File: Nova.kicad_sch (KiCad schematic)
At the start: 35 parts, among them J1 MEM2067-02-180-00-A, J2 Breakout, J3 TC2030-NL, Q1 BC817, Q2 BC817, SW1 PTS636 SK25J, U1 STM32L552RCT6, U2 W25N01GVZEIG, U3 FM24CL16B, Y1 ECS-160-9-33B-CTP-TR, Y2 ECS-.327-9-12R-TR

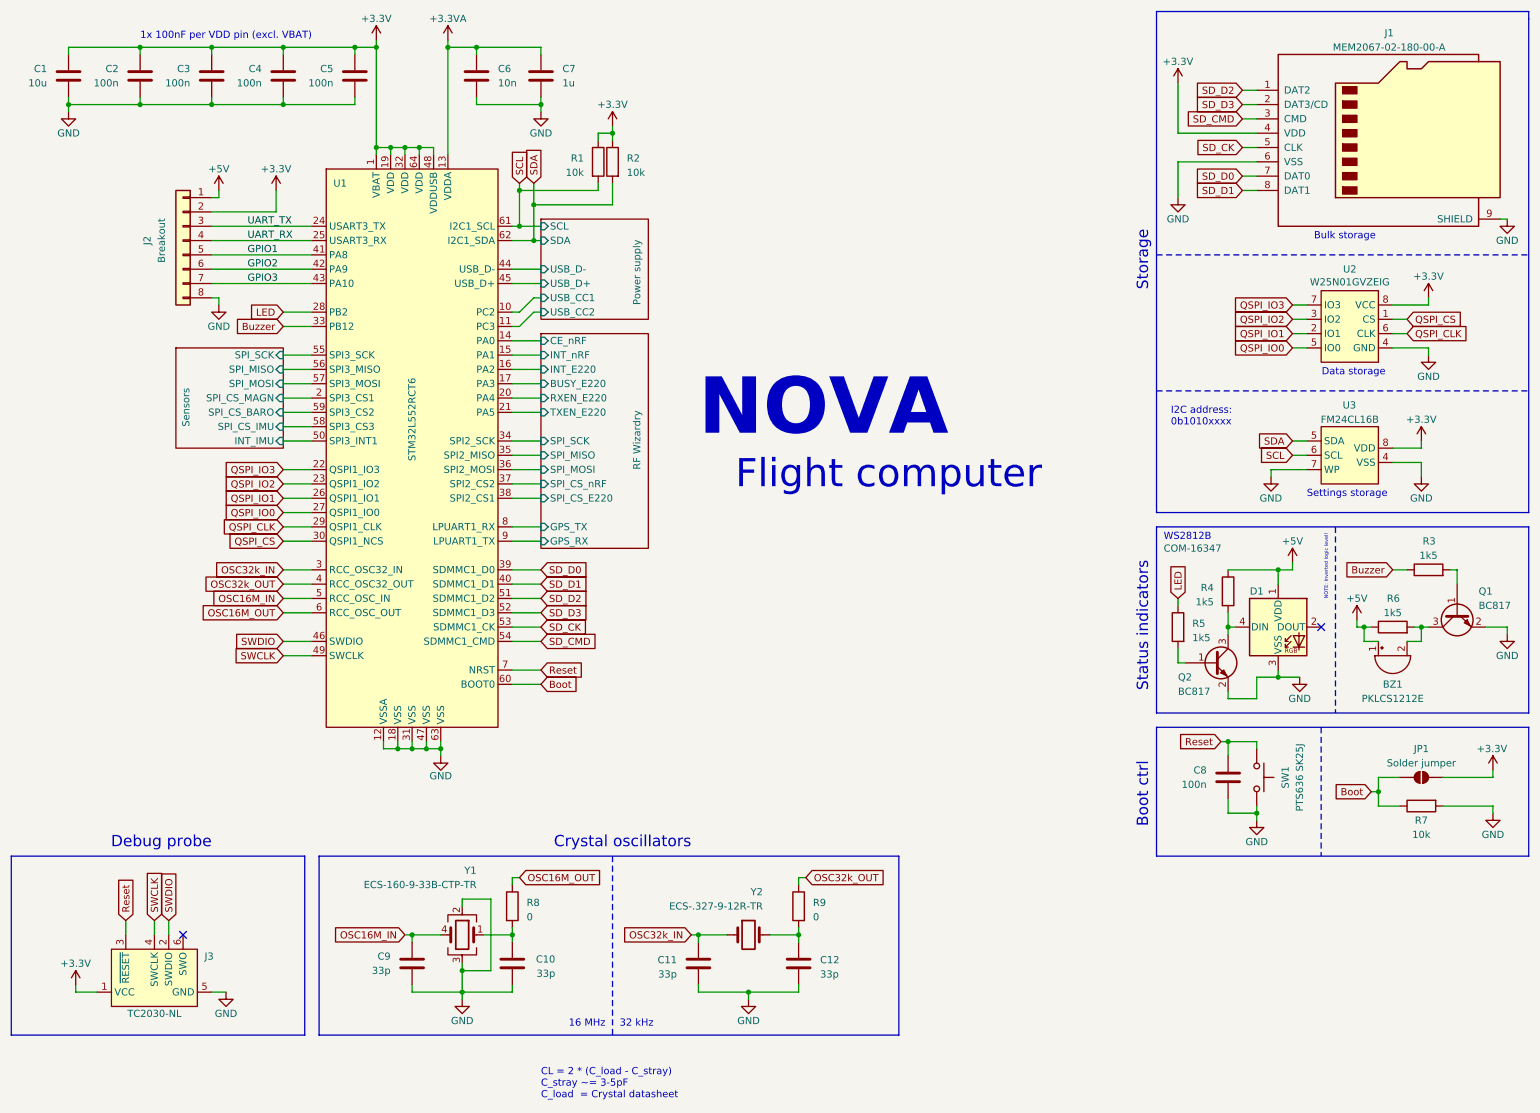
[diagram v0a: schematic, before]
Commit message: :children_crossing: Add test pads and assign footprints
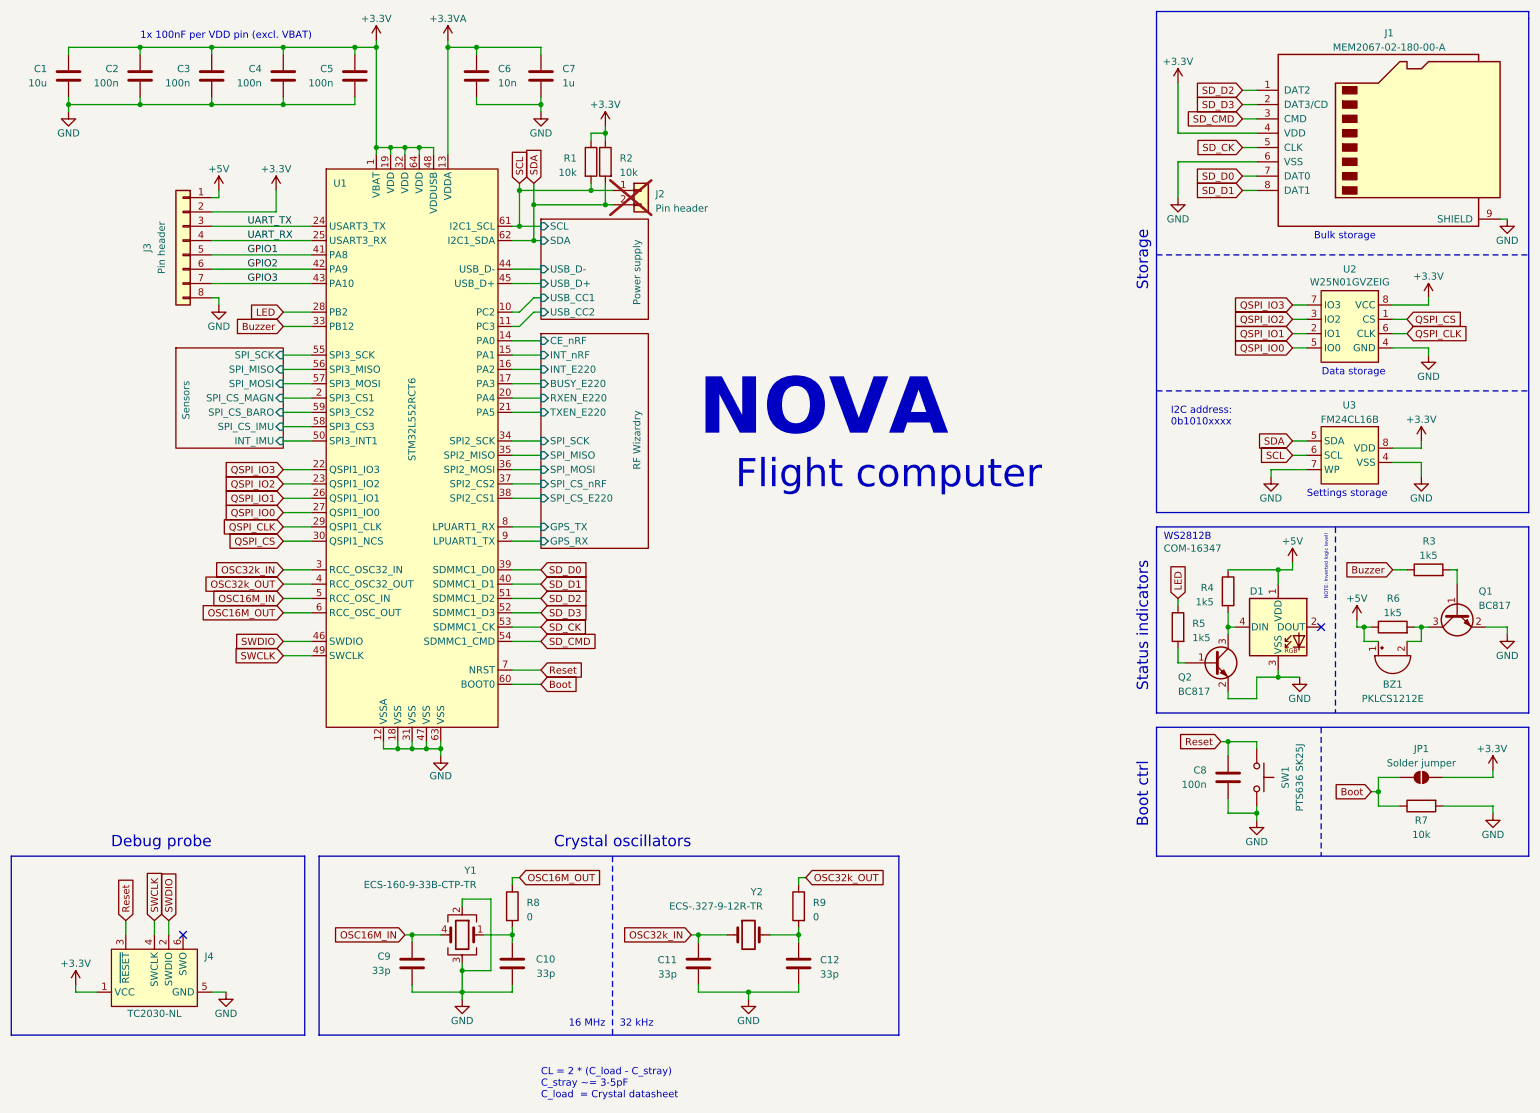
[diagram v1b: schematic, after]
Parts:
- added J2: Pin header, Connector_PinHeader_2.54mm:PinHeader_1x02_P2.54mm_Vertical, symbol Connector_Generic:Conn_01x02
- J3: renamed from J2; value Breakout -> Pin header
- U3: footprint (none) -> Package_SO:SOIC-8_3.9x4.9mm_P1.27mm
- renumbered J3 to J4
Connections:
- net SCL: now also J2.1 (Pin_1)
- net SDA: now also J2.2 (Pin_2)
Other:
- moved on the sheet: R1, R2
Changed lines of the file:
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@@
   (junction (at 93.98 184.15) (diameter 0) (color 0 0 0 0)
   )
+  (junction (at 119.38 48.26) (diameter 0) (color 0 0 0 0)
+  )
   (junction (at 85.09 177.8) (diameter 0) (color 0 0 0 0)
   )
@@
   (junction (at 229.87 123.19) (diameter 0) (color 0 0 0 0)
   )
+  (junction (at 119.38 35.56) (diameter 0) (color 0 0 0 0)
+  )
   (junction (at 229.87 143.51) (diameter 0) (color 0 0 0 0)
   )
@@
   (junction (at 104.14 45.72) (diameter 0) (color 0 0 0 0)
   )
+  (junction (at 116.84 45.72) (diameter 0) (color 0 0 0 0)
+  )
   (junction (at 256.54 152.4) (diameter 0) (color 0 0 0 0)
   )
@@
   )
   (junction (at 36.83 20.32) (diameter 0) (color 0 0 0 0)
-  )
-  (junction (at 120.65 35.56) (diameter 0) (color 0 0 0 0)
   )
   (junction (at 86.36 38.1) (diameter 0) (color 0 0 0 0)
@@
     (stroke (width 0) (type default))
   )
-  (wire (pts (xy 118.11 35.56) (xy 118.11 36.83))
-    (stroke (width 0) (type default))
-  )
   (wire (pts (xy 102.87 80.01) (xy 107.95 80.01))
     (stroke (width 0) (type default))
@@
     (stroke (width 0) (type default))
   )
-  (wire (pts (xy 118.11 45.72) (xy 118.11 44.45))
+  (wire (pts (xy 116.84 45.72) (xy 116.84 44.45))
     (stroke (width 0) (type default))
   )
@@
     (stroke (width 0) (type default))
   )
-  (wire (pts (xy 120.65 36.83) (xy 120.65 35.56))
-    (stroke (width 0) (type default))
-  )
   (wire (pts (xy 269.24 113.03) (xy 270.51 113.03))
     (stroke (width 0) (type default))
@@
     (stroke (width 0) (type default))
   )
-  (wire (pts (xy 106.68 48.26) (xy 120.65 48.26))
+  (wire (pts (xy 106.68 48.26) (xy 119.38 48.26))
     (stroke (width 0) (type default))
   )
@@
     (stroke (width 0) (type default))
   )
+  (wire (pts (xy 119.38 48.26) (xy 120.65 48.26))
+    (stroke (width 0) (type default))
+  )
   (wire (pts (xy 241.3 73.66) (xy 243.84 73.66))
     (stroke (width 0) (type default))
@@
     (stroke (width 0) (type default))
   )
+  (wire (pts (xy 116.84 36.83) (xy 116.84 35.56))
+    (stroke (width 0) (type default))
+  )
   (wire (pts (xy 264.16 125.73) (xy 264.16 123.19))
     (stroke (width 0) (type default))
@@
     (stroke (width 0) (type default))
   )
+  (wire (pts (xy 119.38 35.56) (xy 119.38 36.83))
+    (stroke (width 0) (type default))
+  )
   (wire (pts (xy 106.68 44.45) (xy 106.68 48.26))
     (stroke (width 0) (type default))
@@
   )
   (wire (pts (xy 62.23 30.48) (xy 49.53 30.48))
-    (stroke (width 0) (type default))
-  )
-  (wire (pts (xy 120.65 35.56) (xy 118.11 35.56))
     (stroke (width 0) (type default))
   )
@@
     (stroke (width 0) (type default))
   )
-  (wire (pts (xy 120.65 34.29) (xy 120.65 35.56))
-    (stroke (width 0) (type default))
-  )
   (wire (pts (xy 62.23 67.31) (xy 67.31 67.31))
     (stroke (width 0) (type default))
@@
     (stroke (width 0) (type default))
   )
-  (wire (pts (xy 104.14 45.72) (xy 118.11 45.72))
+  (wire (pts (xy 104.14 45.72) (xy 116.84 45.72))
     (stroke (width 0) (type default))
   )
@@
     (stroke (width 0) (type default))
   )
-  (wire (pts (xy 120.65 44.45) (xy 120.65 48.26))
+  (wire (pts (xy 119.38 44.45) (xy 119.38 48.26))
+    (stroke (width 0) (type default))
+  )
+  (wire (pts (xy 116.84 35.56) (xy 119.38 35.56))
     (stroke (width 0) (type default))
   )
@@
     (stroke (width 0) (type default))
   )
+  (wire (pts (xy 119.38 34.29) (xy 119.38 35.56))
+    (stroke (width 0) (type default))
+  )
   (wire (pts (xy 97.79 177.8) (xy 102.87 177.8))
     (stroke (width 0) (type default))
@@
   )
   (wire (pts (xy 134.62 177.8) (xy 135.89 177.8))
+    (stroke (width 0) (type default))
+  )
+  (wire (pts (xy 116.84 45.72) (xy 120.65 45.72))
     (stroke (width 0) (type default))
   )
@@
   (symbol (lib_id "Connector_Generic:Conn_01x08") (at 44.45 54.61 0) (mirror y) (unit 1)
     (in_bom yes) (on_board yes) (dnp no)
-    (property "Reference" "J2" (at 38.1 54.61 90)
-      (effects (font (size 1.27 1.27)))
-    )
-    (property "Value" "Breakout" (at 40.64 54.61 90)
+    (property "Reference" "J3" (at 38.1 55.88 90)
+      (effects (font (size 1.27 1.27)))
+    )
+    (property "Value" "Pin header" (at 40.64 55.88 90)
       (effects (font (size 1.27 1.27)))
     )
@@
       (project "Nova"
         (path "/0c006d9f-ae30-49aa-ab15-ff0bec4de0e8"
-          (reference "J2") (unit 1)
+          (reference "J3") (unit 1)
         )
       )
@@
   (symbol (lib_id "Connector:Conn_ARM_SWD_TagConnect_TC2030-NL") (at 39.37 185.42 90) (unit 1)
     (in_bom yes) (on_board yes) (dnp no)
-    (property "Reference" "J3" (at 48.26 181.61 90)
+    (property "Reference" "J4" (at 48.26 181.61 90)
       (effects (font (size 1.27 1.27)) (justify right))
     )
@@
       (project "Nova"
         (path "/0c006d9f-ae30-49aa-ab15-ff0bec4de0e8"
-          (reference "J3") (unit 1)
+          (reference "J4") (unit 1)
         )
       )
@@
     )
   )
-  (symbol (lib_id "power:+3.3V") (at 120.65 34.29 0) (unit 1)
-    (in_bom yes) (on_board yes) (dnp no)
-    (property "Reference" "#PWR06" (at 120.65 38.1 0)
-      (effects (font (size 1.27 1.27)) hide)
-    )
-    (property "Value" "+3.3V" (at 120.65 30.48 0)
-      (effects (font (size 1.27 1.27)))
-    )
-    (property "Footprint" "" (at 120.65 34.29 0)
-      (effects (font (size 1.27 1.27)) hide)
-    )
-    (property "Datasheet" "" (at 120.65 34.29 0)
+  (symbol (lib_id "power:+3.3V") (at 119.38 34.29 0) (unit 1)
+    (in_bom yes) (on_board yes) (dnp no)
+    (property "Reference" "#PWR06" (at 119.38 38.1 0)
+      (effects (font (size 1.27 1.27)) hide)
+    )
+    (property "Value" "+3.3V" (at 119.38 30.48 0)
+      (effects (font (size 1.27 1.27)))
+    )
+    (property "Footprint" "" (at 119.38 34.29 0)
+      (effects (font (size 1.27 1.27)) hide)
+    )
+    (property "Datasheet" "" (at 119.38 34.29 0)
       (effects (font (size 1.27 1.27)) hide)
     )
@@
       (effects (font (size 1.27 1.27)))
     )
-    (property "Footprint" "" (at 252.73 87.63 0)
+    (property "Footprint" "Package_SO:SOIC-8_3.9x4.9mm_P1.27mm" (at 252.73 87.63 0)
       (effects (font (size 1.27 1.27)) hide)
     )
@@
         (path "/0c006d9f-ae30-49aa-ab15-ff0bec4de0e8"
           (reference "R7") (unit 1)
+        )
+      )
+    )
+  )
+  (symbol (lib_id "Connector_Generic:Conn_01x02") (at 125.73 45.72 0) (unit 1)
+    (in_bom yes) (on_board yes) (dnp yes) (fields_autoplaced)
+    (property "Reference" "J2" (at 128.27 46.355 0)
+      (effects (font (size 1.27 1.27)) (justify left))
+    )
+    (property "Value" "Pin header" (at 128.27 48.895 0)
+      (effects (font (size 1.27 1.27)) (justify left))
+    )
+    (property "Footprint" "Connector_PinHeader_2.54mm:PinHeader_1x02_P2.54mm_Vertical" (at 125.73 45.72 0)
+      (effects (font (size 1.27 1.27)) hide)
+    )
+    (property "Datasheet" "~" (at 125.73 45.72 0)
+      (effects (font (size 1.27 1.27)) hide)
+    )
+    (pin "1")
+    (pin "2")
+    (instances
+      (project "Nova"
+        (path "/0c006d9f-ae30-49aa-ab15-ff0bec4de0e8"
+          (reference "J2") (unit 1)
         )
       )
@@
     )
   )
-  (symbol (lib_id "Device:R") (at 118.11 40.64 0) (unit 1)
-    (in_bom yes) (on_board yes) (dnp no)
-    (property "Reference" "R1" (at 115.57 40.005 0)
+  (symbol (lib_id "Device:R") (at 116.84 40.64 0) (unit 1)
+    (in_bom yes) (on_board yes) (dnp no)
+    (property "Reference" "R1" (at 114.3 40.005 0)
       (effects (font (size 1.27 1.27)) (justify right))
     )
-    (property "Value" "10k" (at 115.57 42.545 0)
+    (property "Value" "10k" (at 114.3 42.545 0)
       (effects (font (size 1.27 1.27)) (justify right))
     )
-    (property "Footprint" "Resistor_SMD:R_0402_1005Metric_Pad0.72x0.64mm_HandSolder" (at 116.332 40.64 90)
-      (effects (font (size 1.27 1.27)) hide)
-    )
-    (property "Datasheet" "~" (at 118.11 40.64 0)
+    (property "Footprint" "Resistor_SMD:R_0402_1005Metric_Pad0.72x0.64mm_HandSolder" (at 115.062 40.64 90)
+      (effects (font (size 1.27 1.27)) hide)
+    )
+    (property "Datasheet" "~" (at 116.84 40.64 0)
       (effects (font (size 1.27 1.27)) hide)
     )
@@
     )
   )
-  (symbol (lib_id "Device:R") (at 120.65 40.64 0) (mirror y) (unit 1)
+  (symbol (lib_id "Device:R") (at 119.38 40.64 0) (mirror y) (unit 1)
     (in_bom yes) (on_board yes) (dnp no) (fields_autoplaced)
-    (property "Reference" "R2" (at 123.19 40.005 0)
+    (property "Reference" "R2" (at 121.92 40.005 0)
       (effects (font (size 1.27 1.27)) (justify right))
     )
-    (property "Value" "10k" (at 123.19 42.545 0)
+    (property "Value" "10k" (at 121.92 42.545 0)
       (effects (font (size 1.27 1.27)) (justify right))
     )
-    (property "Footprint" "Resistor_SMD:R_0402_1005Metric_Pad0.72x0.64mm_HandSolder" (at 122.428 40.64 90)
-      (effects (font (size 1.27 1.27)) hide)
-    )
-    (property "Datasheet" "~" (at 120.65 40.64 0)
+    (property "Footprint" "Resistor_SMD:R_0402_1005Metric_Pad0.72x0.64mm_HandSolder" (at 121.158 40.64 90)
+      (effects (font (size 1.27 1.27)) hide)
+    )
+    (property "Datasheet" "~" (at 119.38 40.64 0)
       (effects (font (size 1.27 1.27)) hide)
     )
@@
     (stroke (width 0.1524) (type solid))
     (fill (color 255 175 0 0.1500))
-    (property "Sheetname" "Sensors" (at 45.72 87.63 90)
+    (property "Sheetname" "Sensors" (at 45.72 86.36 90)
       (effects (font (size 1.27 1.27)) (justify left bottom))
     )
